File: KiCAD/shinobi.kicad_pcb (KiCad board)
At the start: 13 copper layers, 49.9 x 47 mm, 111 parts, among them J1 61300211121, J2 217179-0001, J3 61301011121, J4 61300711121, Q1 PUMH13-QF, U1 TPS62825DMQR, U2 TPS62825DMQR, U3 CH343P, U4 ESP8285, U5 74LVC2G17GW-Q100H, U6 SI5351A, U7 TV5725, U8 W9864G2JH-6, Y1 26MHz 10pF 2520, Y2 25MHz 10pF 2520, Y3 27MHz 10pF 2520

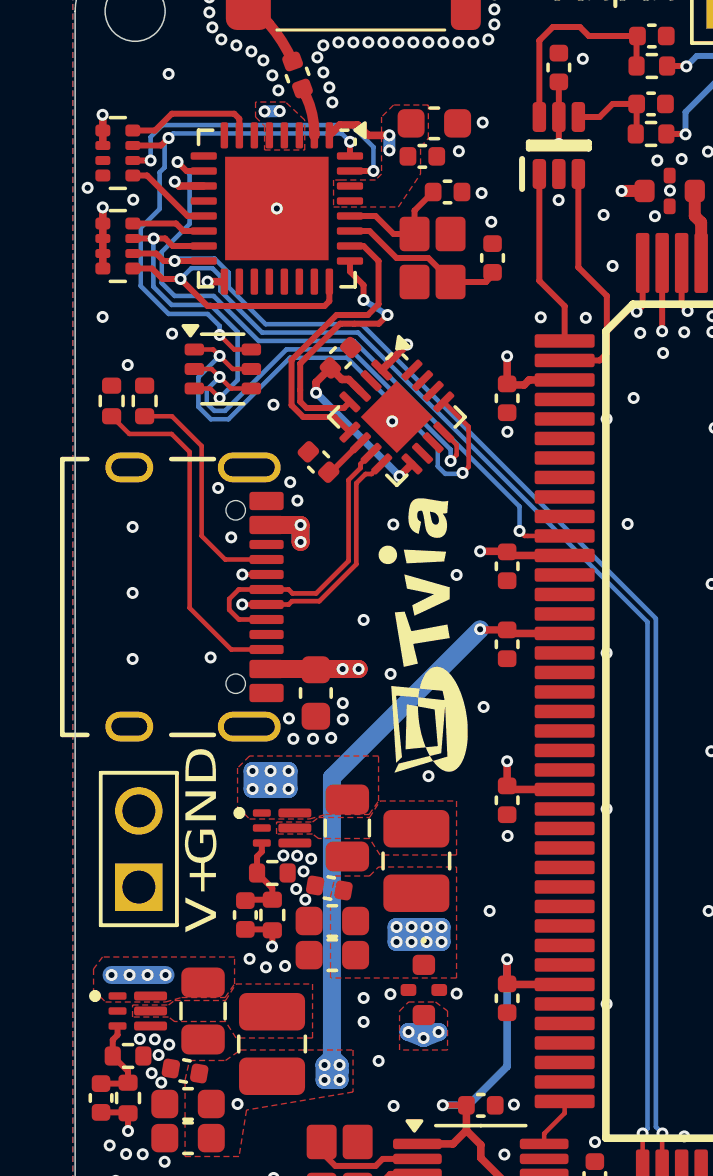
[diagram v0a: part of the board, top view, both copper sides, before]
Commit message: embed fonts, layout tweaks
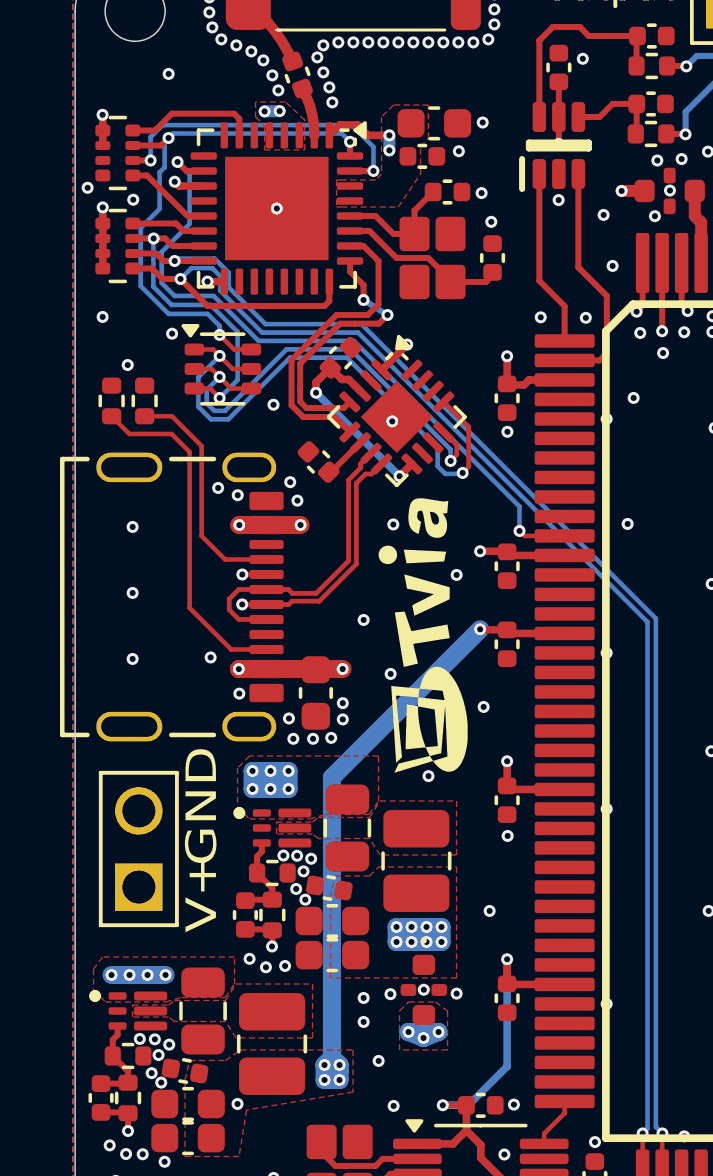
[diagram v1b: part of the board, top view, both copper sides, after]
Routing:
- net +1V5: track 36.6 -> 39.3 mm
- net VBUS: track 28.0 -> 26.5 mm
- net GND: vias 225 -> 227
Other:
- copper layers 13 -> 4

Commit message: more minor layout tweaks
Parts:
- moved Y3 1.21 mm to (167.0, 87.8)
- moved C52 1.21 mm to (164.8, 87.8)
- moved C54 1.21 mm to (169.3, 87.8)
- moved R22 1.21 mm to (167.3, 89.7)
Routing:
- net Net-(U7-XTOUT): track 6.59 -> 5.64 mm
- net Net-(U7-XTIN): track 7.95 -> 7.09 mm
- net GND: vias 227 -> 226
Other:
- outline, holes or cut-outs redrawn
